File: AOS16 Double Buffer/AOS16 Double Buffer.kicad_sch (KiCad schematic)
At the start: 18 parts, among them J1 Conn_01x02_Pin, J6 Conn_01x07_Pin, U1 74LVC1G08, U2 74LVC1G08, U3 74LVC1G32, U4 74LVC1G32, U5 74LVC1G04, U6 74LVC1G04, U7 74LVC157

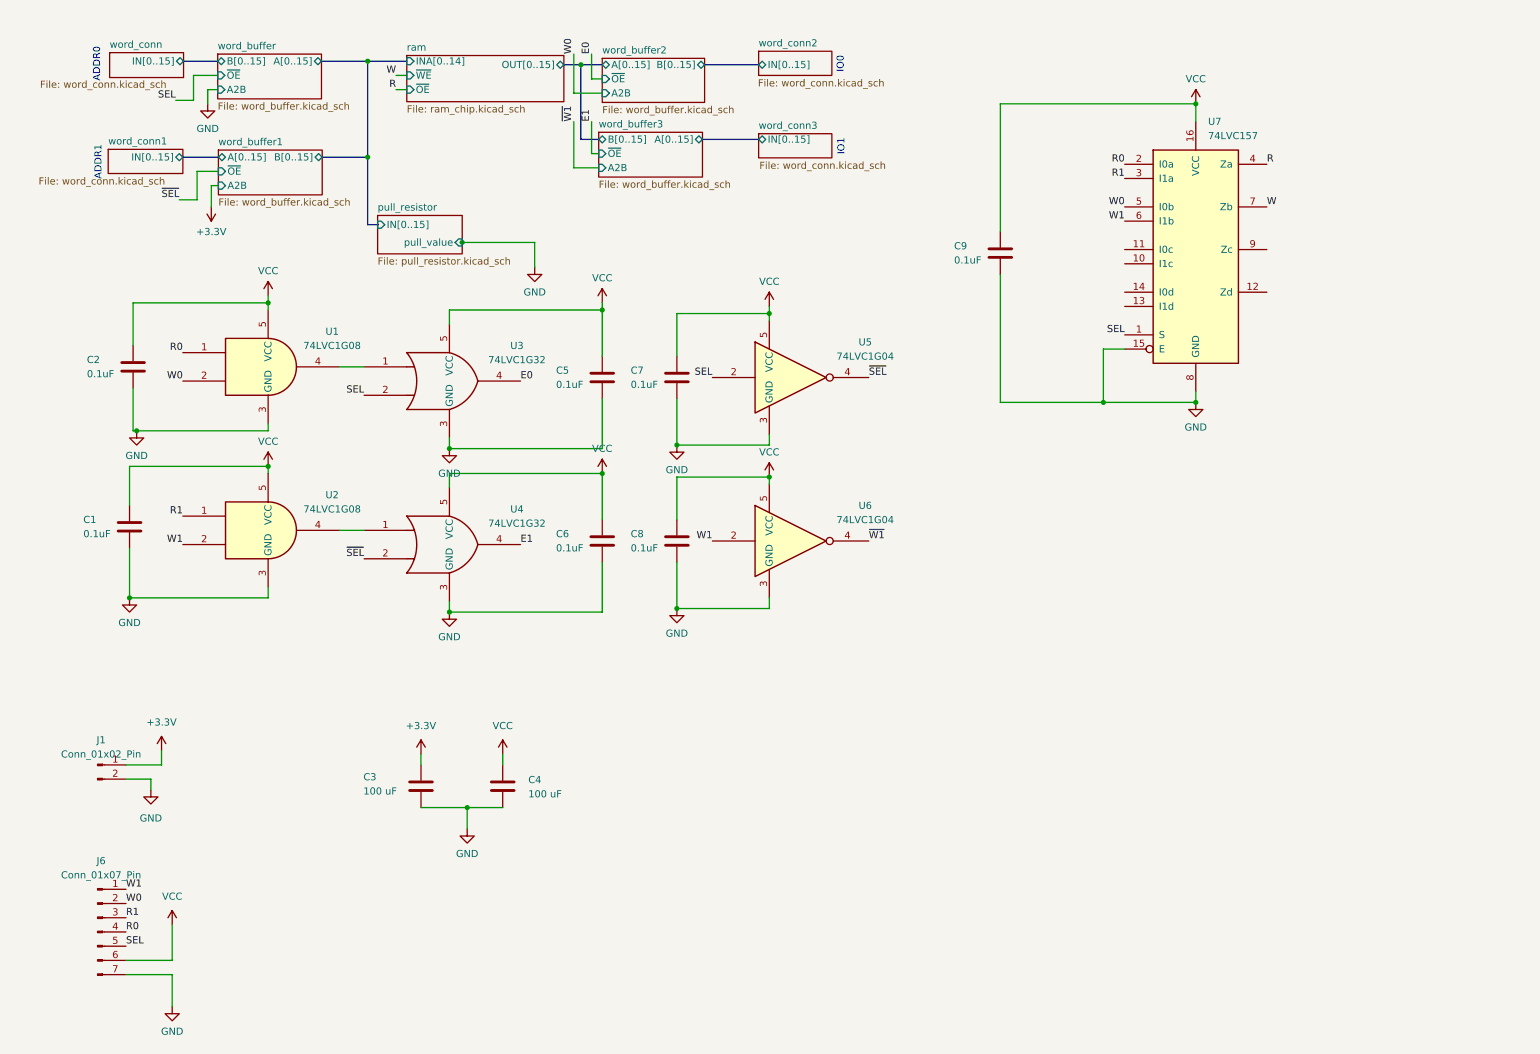
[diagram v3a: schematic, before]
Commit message: Fixed double buffer logic families
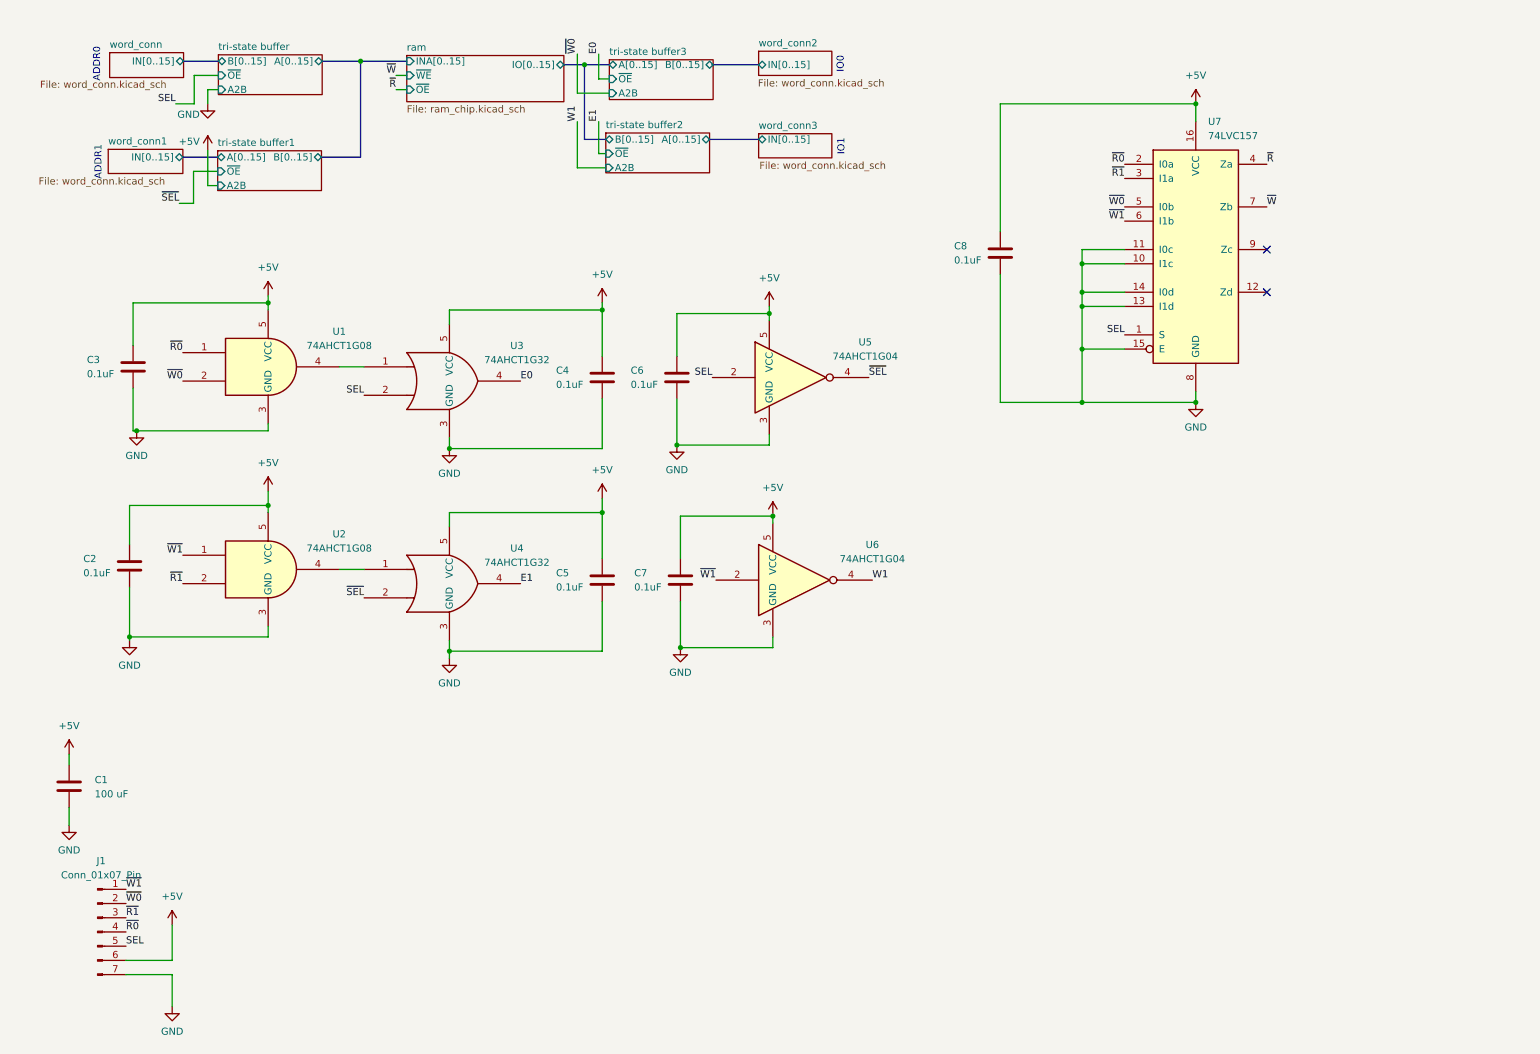
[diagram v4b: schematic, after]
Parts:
- removed C3: 100 uF, Capacitor_SMD:CP_Elec_5x5.3, symbol Device:C
- removed J1: Conn_01x02_Pin, Connector_PinHeader_2.54mm:PinHeader_1x02_P2.54mm_Vertical, symbol Connector:Conn_01x02_Pin
- U1, U2: value 74LVC1G08 -> 74AHCT1G08; footprint Package_TO_SOT_SMD:SOT-353_SC-70-5 -> Package_TO_SOT_SMD:SOT-23-5
- U3, U4: value 74LVC1G32 -> 74AHCT1G32; footprint Package_TO_SOT_SMD:SOT-353_SC-70-5 -> Package_TO_SOT_SMD:SOT-23-5
- U5, U6: value 74LVC1G04 -> 74AHCT1G04; footprint Package_TO_SOT_SMD:SOT-353_SC-70-5 -> Package_TO_SOT_SMD:SOT-23-5
- renumbered C4 to C1, C1 to C2, C2 to C3, C5 to C4, C6 to C5, C7 to C6, C8 to C7, C9 to C8, J6 to J1
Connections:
- net GND: now also U7.10 (I1c), U7.11 (I0c), U7.13 (I1d), U7.14 (I0d)
- net W1: now also U6.4; no longer J1.1 (Pin_1), U2.2, U6.2, U7.6 (I1b)
- net ~{W1}: now also J1.1 (Pin_1), U2.1, U6.2, U7.6 (I1b); no longer U6.4
- net R renamed ~{R}
- net R0 renamed ~{R0}
- net R1 renamed ~{R1}
- net ~{R1}: now also U2.2; no longer U2.1
- net VCC renamed +5V
- net W renamed ~{W}
- net W0 renamed ~{W0}
- no-connect marks 0 -> 2
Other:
- removed sheet pull_resistor
- removed sheet word_buffer
- removed sheet word_buffer1
- removed sheet word_buffer2
- removed sheet word_buffer3
- added sheet tri-state buffer (../common/tri-state buffer16.kicad_sch)
- added sheet tri-state buffer1 (../common/tri-state buffer16.kicad_sch)
- added sheet tri-state buffer2 (../common/tri-state buffer16.kicad_sch)
- added sheet tri-state buffer3 (../common/tri-state buffer16.kicad_sch)
- sheet ram ports: added INA[0..15], IO[0..15]; removed INA[0..14], OUT[0..15]
- moved on the sheet: C1, C2, C5, C7, U2, U4, U6

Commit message: Fixed tri-state buffer and completed double buffer PCB
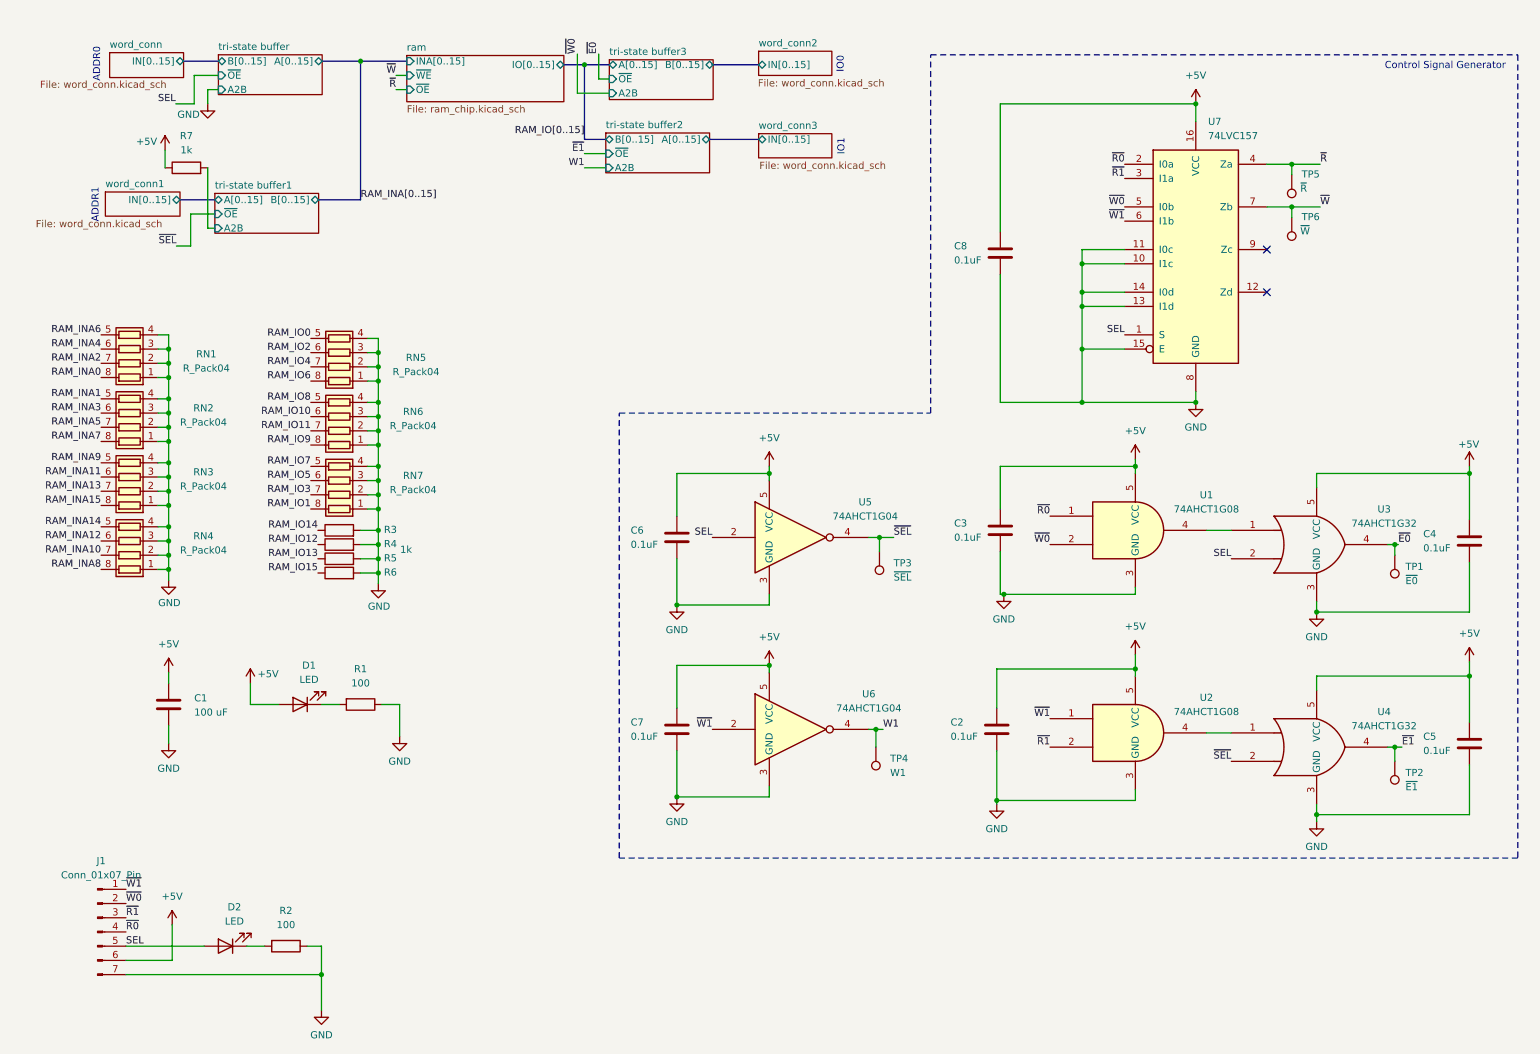
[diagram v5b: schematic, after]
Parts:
- added D1, D2: LED, LED_SMD:LED_0603_1608Metric, symbol Device:LED
- added R1, R2: 100, Resistor_SMD:R_0603_1608Metric, symbol Device:R
- added R3, R4, R5, R6, R7: 1k, Resistor_SMD:R_0603_1608Metric, symbol Device:R
- added RN1, RN2, RN3, RN4, RN5, RN6, RN7: R_Pack04, Resistor_SMD:R_Cat16-4, symbol Device:R_Pack04
- added TP1: ~{E0}, TestPoint:TestPoint_Pad_D1.0mm, symbol Connector:TestPoint
- added TP2: ~{E1}, TestPoint:TestPoint_Pad_D1.0mm, symbol Connector:TestPoint
- added TP3: ~{SEL}, TestPoint:TestPoint_Pad_D1.0mm, symbol Connector:TestPoint
- added TP4: W1, TestPoint:TestPoint_Pad_D1.0mm, symbol Connector:TestPoint
- added TP5: ~{R}, TestPoint:TestPoint_Pad_D1.0mm, symbol Connector:TestPoint
- added TP6: ~{W}, TestPoint:TestPoint_Pad_D1.0mm, symbol Connector:TestPoint
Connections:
- net +5V: now also D1.2 (A), R7.1
- net GND: now also R1.1, R2.1, R3.2, R4.2, R5.2, R6.2, RN1.1 (R1.1), RN1.2 (R2.1), RN1.3 (R3.1), RN1.4 (R4.1), RN2.1 (R1.1), RN2.2 (R2.1), RN2.3 (R3.1), RN2.4 (R4.1), RN3.1 (R1.1), RN3.2 (R2.1), RN3.3 (R3.1), RN3.4 (R4.1), RN4.1 (R1.1), RN4.2 (R2.1), RN4.3 (R3.1), RN4.4 (R4.1), RN5.1 (R1.1), RN5.2 (R2.1), RN5.3 (R3.1), RN5.4 (R4.1), RN6.1 (R1.1), RN6.2 (R2.1), RN6.3 (R3.1), RN6.4 (R4.1), RN7.1 (R1.1), RN7.2 (R2.1), RN7.3 (R3.1), RN7.4 (R4.1)
- net SEL: now also D2.2 (A)
- net W1: now also TP4.1
- net ~{R}: now also TP5.1
- net ~{SEL}: now also TP3.1
- net ~{W}: now also TP6.1
- net E0 renamed ~{E0}
- net ~{E0}: now also TP1.1
- net E1 renamed ~{E1}
- net ~{E1}: now also TP2.1
- new net: D2.1 (K), R2.2
- new net: D1.1 (K), R1.2
- new net RAM_INA0: RN1.8 (R1.2)
- new net RAM_INA1: RN2.5 (R4.2)
- new net RAM_INA10: RN4.7 (R2.2)
- new net RAM_INA11: RN3.6 (R3.2)
- new net RAM_INA12: RN4.6 (R3.2)
- new net RAM_INA13: RN3.7 (R2.2)
- new net RAM_INA14: RN4.5 (R4.2)
- new net RAM_INA15: RN3.8 (R1.2)
- new net RAM_INA2: RN1.7 (R2.2)
- new net RAM_INA3: RN2.6 (R3.2)
- new net RAM_INA4: RN1.6 (R3.2)
- new net RAM_INA5: RN2.7 (R2.2)
- new net RAM_INA6: RN1.5 (R4.2)
- new net RAM_INA7: RN2.8 (R1.2)
- new net RAM_INA8: RN4.8 (R1.2)
- new net RAM_INA9: RN3.5 (R4.2)
- new net RAM_IO0: RN5.5 (R4.2)
- new net RAM_IO1: RN7.8 (R1.2)
- new net RAM_IO10: RN6.6 (R3.2)
- new net RAM_IO11: RN6.7 (R2.2)
- new net RAM_IO12: R4.1
- new net RAM_IO13: R5.1
- new net RAM_IO14: R3.1
- new net RAM_IO15: R6.1
- new net RAM_IO2: RN5.6 (R3.2)
- new net RAM_IO3: RN7.7 (R2.2)
- new net RAM_IO4: RN5.7 (R2.2)
- new net RAM_IO5: RN7.6 (R3.2)
- new net RAM_IO6: RN5.8 (R1.2)
- new net RAM_IO7: RN7.5 (R4.2)
- new net RAM_IO8: RN6.5 (R4.2)
- new net RAM_IO9: RN6.8 (R1.2)
- new net tri-state buffer1/A2B: R7.2
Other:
- note added: "Control Signal Generator"
- moved on the sheet: C1, C2, C3, C4, C5, C6, C7, U1, U2, U3, U4, U5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

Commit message: Memory Controller- Initial setup
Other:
- sheet ram: file ram_chip.kicad_sch -> ../common/ram_chip.kicad_sch
- sheet word_conn: file word_conn.kicad_sch -> ../common/word_conn.kicad_sch
- sheet word_conn1: file word_conn.kicad_sch -> ../common/word_conn.kicad_sch
- sheet word_conn2: file word_conn.kicad_sch -> ../common/word_conn.kicad_sch
- sheet word_conn3: file word_conn.kicad_sch -> ../common/word_conn.kicad_sch
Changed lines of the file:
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@@
 (kicad_sch
-	(version 20231120)
+	(version 20250114)
 	(generator "eeschema")
-	(generator_version "8.0")
+	(generator_version "9.0")
 	(paper "A4")
+	(text "ADDR1\n\n\n\n"
+		(exclude_from_sim no)
+		(at 28.067 46.736 90)
+		(effects
+			(font
+				(size 1.27 1.27)
+			)
+		)
+	)
+	(text "Control Signal Generator\n"
+		(exclude_from_sim no)
+		(at 266.192 21.844 0)
+		(effects
+			(font
+				(size 1.27 1.27)
+			)
+		)
+	)
+	(text "IO1\n"
+		(exclude_from_sim no)
+		(at 158.242 36.322 90)
+		(effects
+			(font
+				(size 1.27 1.27)
+			)
+		)
+	)
+	(text "ADDR0\n\n\n"
+		(exclude_from_sim no)
+		(at 27.305 21.59 90)
+		(effects
+			(font
+				(size 1.27 1.27)
+			)
+		)
+	)
+	(text "IO0\n"
+		(exclude_from_sim no)
+		(at 158.115 21.59 90)
+		(effects
+			(font
+				(size 1.27 1.27)
+			)
+		)
+	)
 	(junction
 		(at 210.82 93.345)
@@
 		)
 	)
-	(text "ADDR1\n\n\n\n"
-		(exclude_from_sim no)
-		(at 28.067 46.736 90)
-		(effects
-			(font
-				(size 1.27 1.27)
-			)
-		)
-	)
-	(text "Control Signal Generator\n"
-		(exclude_from_sim no)
-		(at 266.192 21.844 0)
-		(effects
-			(font
-				(size 1.27 1.27)
-			)
-		)
-	)
-	(text "IO1\n"
-		(exclude_from_sim no)
-		(at 158.242 36.322 90)
-		(effects
-			(font
-				(size 1.27 1.27)
-			)
-		)
-	)
-	(text "ADDR0\n\n\n"
-		(exclude_from_sim no)
-		(at 27.305 21.59 90)
-		(effects
-			(font
-				(size 1.27 1.27)
-			)
-		)
-	)
-	(text "IO0\n"
-		(exclude_from_sim no)
-		(at 158.115 21.59 90)
-		(effects
-			(font
-				(size 1.27 1.27)
-			)
-		)
-	)
 	(label "RAM_INA13"
 		(at 26.035 97.79 180)
@@
 	(label "~{SEL}"
 		(at 227.965 146.05 180)
-		(fields_autoplaced yes)
 		(effects
 			(font
@@
 	(label "~{R0}"
 		(at 208.915 39.37 180)
-		(fields_autoplaced yes)
 		(effects
 			(font
@@
 	(label "~{W0}"
 		(at 111.125 19.685 90)
-		(fields_autoplaced yes)
 		(effects
 			(font
@@
 	(label "~{R}"
 		(at 243.84 39.37 0)
-		(fields_autoplaced yes)
 		(effects
 			(font
@@
 	(label "~{W0}"
 		(at 208.915 46.99 180)
-		(fields_autoplaced yes)
 		(effects
 			(font
@@
 	(label "RAM_IO[0..15]"
 		(at 112.395 34.29 180)
-		(fields_autoplaced yes)
 		(effects
 			(font
@@
 	(label "~{W}"
 		(at 243.84 46.99 0)
-		(fields_autoplaced yes)
 		(effects
 			(font
@@
 	(label "SEL"
 		(at 39.37 28.575 180)
-		(fields_autoplaced yes)
 		(effects
 			(font
@@
 	(label "~{R0}"
 		(at 30.48 176.53 0)
-		(fields_autoplaced yes)
 		(effects
 			(font
@@
 	(label "SEL"
 		(at 208.915 69.85 180)
-		(fields_autoplaced yes)
 		(effects
 			(font
@@
 	(label "RAM_INA0"
 		(at 26.035 77.47 180)
-		(fields_autoplaced yes)
 		(effects
 			(font
@@
 	(label "W1"
 		(at 165.735 140.335 0)
-		(fields_autoplaced yes)
 		(effects
 			(font
@@
 	(label "RAM_INA4"
 		(at 26.035 72.39 180)
-		(fields_autoplaced yes)
 		(effects
 			(font
@@
 	(label "RAM_INA[0..15]"
 		(at 72.39 45.72 0)
-		(fields_autoplaced yes)
 		(effects
 			(font
@@
 	(label "~{E0}"
 		(at 114.935 19.685 90)
-		(fields_autoplaced yes)
 		(effects
 			(font
@@
 	(label "RAM_INA2"
 		(at 26.035 74.93 180)
-		(fields_autoplaced yes)
 		(effects
 			(font
@@
 	(label "~{SEL}"
 		(at 167.64 106.045 0)
-		(fields_autoplaced yes)
 		(effects
 			(font
@@
 	(label "~{R1}"
 		(at 208.915 41.91 180)
-		(fields_autoplaced yes)
 		(effects
 			(font
@@
 	(label "~{R1}"
 		(at 30.48 173.99 0)
-		(fields_autoplaced yes)
 		(effects
 			(font
@@
 	(label "~{W0}"
 		(at 30.48 171.45 0)
-		(fields_autoplaced yes)
 		(effects
 			(font
@@
 	(label "~{W}"
 		(at 78.74 23.495 180)
-		(fields_autoplaced yes)
 		(effects
 			(font
@@
 	(label "RAM_INA6"
 		(at 26.035 69.85 180)
-		(fields_autoplaced yes)
 		(effects
 			(font
@@
 	(label "~{W1}"
 		(at 195.58 138.43 180)
-		(fields_autoplaced yes)
 		(effects
 			(font
@@
 	(label "~{R}"
 		(at 78.74 26.035 180)
-		(fields_autoplaced yes)
 		(effects
 			(font
@@
 	(label "~{SEL}"
 		(at 39.497 53.975 180)
-		(fields_autoplaced yes)
 		(effects
 			(font
@@
 	(label "~{W1}"
 		(at 30.48 168.91 0)
-		(fields_autoplaced yes)
 		(effects
 			(font
@@
 	(label "~{R0}"
 		(at 195.58 102.235 180)
-		(fields_autoplaced yes)
 		(effects
 			(font
@@
 	(label "SEL"
 		(at 30.48 179.07 0)
-		(fields_autoplaced yes)
 		(effects
 			(font
@@
 	(label "~{W0}"
 		(at 195.58 107.315 180)
-		(fields_autoplaced yes)
 		(effects
 			(font
@@
 	(label "~{R1}"
 		(at 195.58 143.51 180)
-		(fields_autoplaced yes)
 		(effects
 			(font
@@
 	(label "~{E1}"
 		(at 258.445 143.51 0)
-		(fields_autoplaced yes)
 		(effects
 			(font
@@
 	(label "~{W1}"
 		(at 135.255 140.335 180)
-		(fields_autoplaced yes)
 		(effects
 			(font
@@
 	(label "~{W1}"
 		(at 208.915 49.53 180)
-		(fields_autoplaced yes)
 		(effects
 			(font
@@
 	(label "~{E1}"
 		(at 112.395 37.465 180)
-		(fields_autoplaced yes)
 		(effects
 			(font
@@
 	(label "SEL"
 		(at 135.255 106.045 180)
-		(fields_autoplaced yes)
 		(effects
 			(font
@@
 	(label "~{E0}"
 		(at 257.81 107.315 0)
-		(fields_autoplaced yes)
 		(effects
 			(font
@@
 	(label "W1"
 		(at 112.395 40.005 180)
-		(fields_autoplaced yes)
 		(effects
 			(font
@@
 	(label "SEL"
 		(at 227.965 109.855 180)
-		(fields_autoplaced yes)
 		(effects
 			(font
@@
 		(at 143.51 19.177)
 		(size 13.081 4.318)
+		(exclude_from_sim no)
+		(in_bom yes)
+		(on_board yes)
+		(dnp no)
 		(stroke
 			(width 0.1524)
@@
 			)
 		)
-		(property "Sheetfile" "word_conn.kicad_sch"
+		(property "Sheetfile" "../common/word_conn.kicad_sch"
 			(at 143.383 24.13 0)
 			(effects
@@
 		(at 80.645 19.939)
 		(size 28.067 8.255)
+		(exclude_from_sim no)
+		(in_bom yes)
+		(on_board yes)
+		(dnp no)
 		(fields_autoplaced yes)
 		(stroke
@@
 			)
 		)
-		(property "Sheetfile" "ram_chip.kicad_sch"
+		(property "Sheetfile" "../common/ram_chip.kicad_sch"
 			(at 80.645 28.7786 0)
 			(effects
@@
 		(at 27.559 19.431)
 		(size 13.208 4.445)
+		(exclude_from_sim no)
+		(in_bom yes)
+		(on_board yes)
+		(dnp no)
 		(stroke
 			(width 0.1524)
@@
 			)
 		)
-		(property "Sheetfile" "word_conn.kicad_sch"
+		(property "Sheetfile" "../common/word_conn.kicad_sch"
 			(at 15.113 24.384 0)
 			(effects
@@
 		(at 46.99 19.812)
 		(size 18.542 7.112)
+		(exclude_from_sim no)
+		(in_bom yes)
+		(on_board yes)
+		(dnp no)
 		(fields_autoplaced yes)
 		(stroke
@@
 		(at 143.51 33.909)
 		(size 13.081 4.318)
+		(exclude_from_sim no)
+		(in_bom yes)
+		(on_board yes)
+		(dnp no)
 		(stroke
 			(width 0.1524)
@@
 			)
 		)
-		(property "Sheetfile" "word_conn.kicad_sch"
+		(property "Sheetfile" "../common/word_conn.kicad_sch"
 			(at 143.637 38.862 0)
 			(effects
@@
 		(at 116.205 33.782)
 		(size 18.542 7.112)
+		(exclude_from_sim no)
+		(in_bom yes)
+		(on_board yes)
+		(dnp no)
 		(fields_autoplaced yes)
 		(stroke
@@
 		(at 26.797 44.323)
 		(size 13.335 4.318)
+		(exclude_from_sim no)
+		(in_bom yes)
+		(on_board yes)
+		(dnp no)
 		(stroke
 			(width 0.1524)
@@
 			)
 		)
-		(property "Sheetfile" "word_conn.kicad_sch"
+		(property "Sheetfile" "../common/word_conn.kicad_sch"
 			(at 14.351 49.276 0)
 			(effects
@@
 		(at 116.84 20.701)
 		(size 18.542 7.112)
+		(exclude_from_sim no)
+		(in_bom yes)
+		(on_board yes)
+		(dnp no)
 		(fields_autoplaced yes)
 		(stroke
@@
 		(at 46.355 44.577)
 		(size 18.542 7.112)
+		(exclude_from_sim no)
+		(in_bom yes)
+		(on_board yes)
+		(dnp no)
 		(fields_autoplaced yes)
 		(stroke
@@
 		)
 	)
+	(embedded_fonts no)
 )
